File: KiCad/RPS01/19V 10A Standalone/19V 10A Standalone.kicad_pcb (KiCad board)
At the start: 2 copper layers, 33 parts, among them U2 LTC3780EUH-TRPBF

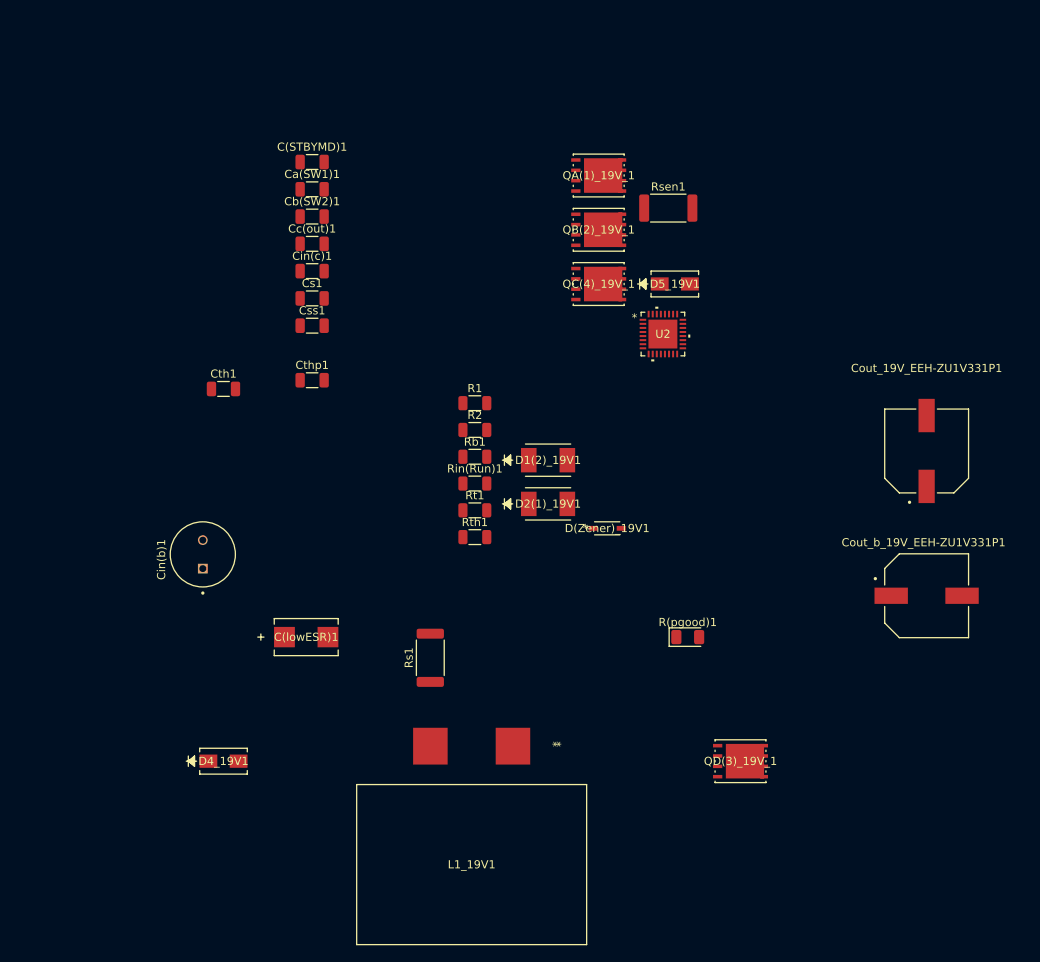
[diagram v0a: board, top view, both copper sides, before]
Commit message: 19V 10A Standalone PCB
Updated the standalone 19V 10A PCB. Just needs the connectors.
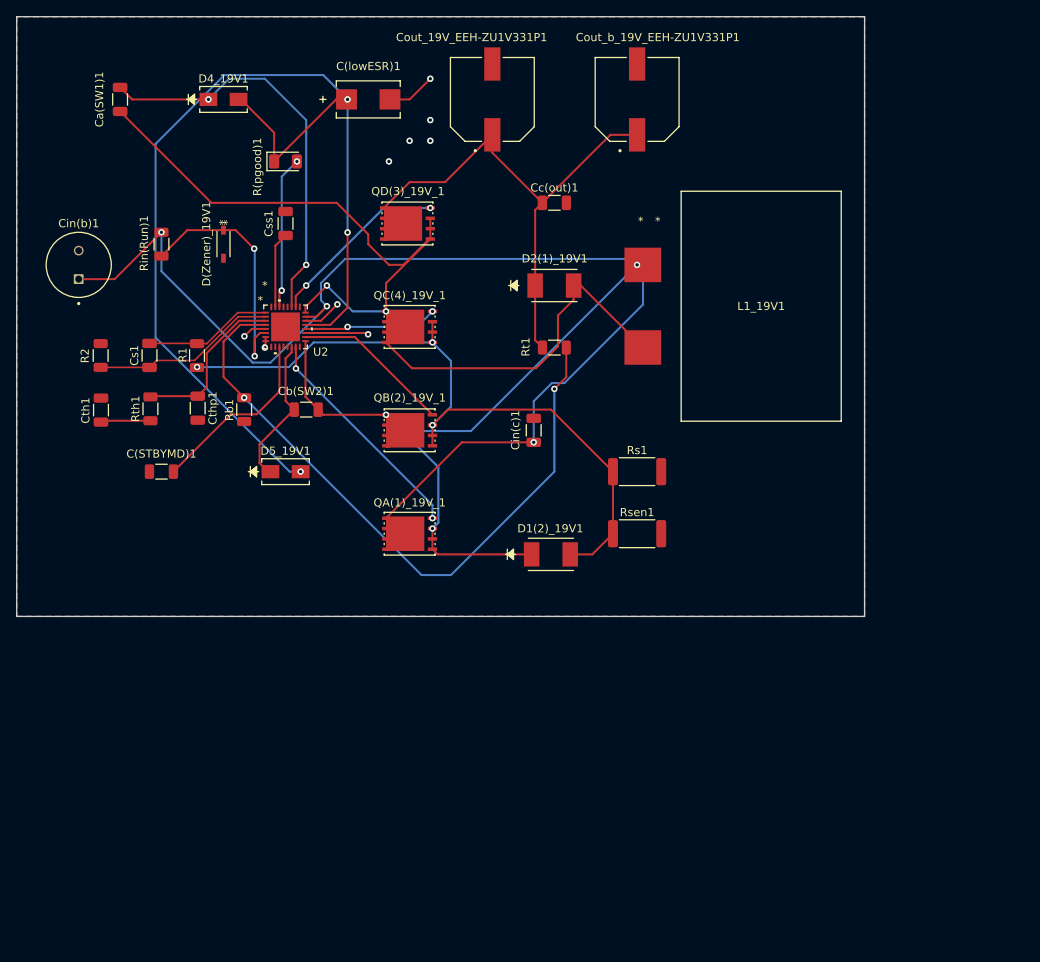
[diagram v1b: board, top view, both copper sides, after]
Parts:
- moved D4_19V1 81.3 mm to (114.3, 45.7)
- moved QD(3)_19V_1 77.7 mm to (136.9, 61.0), turned to 180 degrees
- moved L1_19V1 77.3 mm to (180.3, 71.1), turned to 0 degrees
- moved R(pgood)1 76.5 mm to (121.9, 53.3)
- moved Cout_b_19V_EEH-ZU1V331P1 70.6 mm to (165.1, 45.7), turned to 90 degrees
- moved Cout_19V_EEH-ZU1V331P1 68.6 mm to (147.3, 45.7)
- moved C(lowESR)1 66.5 mm to (132.1, 45.7)
- moved D(Zener)_19V1 58.6 mm to (114.3, 63.5), turned to -90 degrees
- moved D5_19V1 53.1 mm to (121.9, 91.4)
- moved QA(1)_19V_1 49.7 mm to (137.2, 99.1), turned to 180 degrees
- moved Rin(Run)1 48.4 mm to (106.7, 63.5), turned to -90 degrees
- moved R2 46.9 mm to (99.2, 77.2), turned to 90 degrees
- moved U2 46.4 mm to (121.9, 73.7)
- moved Rth1 42.8 mm to (105.3, 83.7), turned to 90 degrees
- moved C(STBYMD)1 42.3 mm to (106.7, 91.4), turned to 180 degrees
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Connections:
- Cb(SW2)1 pad 1: /BOOST2 -> /SW2
- D1(2)_19V1 pad 1: /BOOST2 -> /SW2
- L1_19V1 pad 1: /BOOST2 -> /SW2
- QA(1)_19V_1 pad 1: /BOOST2 -> /SW2
- QA(1)_19V_1 pad 2: /BOOST2 -> /SW2
- QA(1)_19V_1 pad 3: /BOOST2 -> /SW2
- QB(2)_19V_1 pad 5: /BOOST2 -> /SW2
- QB(2)_19V_1 pad 6: /BOOST2 -> /SW2
- QB(2)_19V_1 pad 7: /BOOST2 -> /SW2
- QB(2)_19V_1 pad 8: /BOOST2 -> /SW2
- U2 pad 17: /BOOST2 -> /SW2
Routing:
- net /Vin: track 0.00 -> 143.0 mm, vias 0 -> 3
- net /INTVCC: track 0.00 -> 130.0 mm, vias 0 -> 3
- net /SW1: track 0.00 -> 118.0 mm, vias 0 -> 2
- net /SW2: track 0.00 -> 89.7 mm, vias 0 -> 3
- net /Rsense: track 0.00 -> 87.3 mm, vias 0 -> 3
- net /VOSENSE: track 0.00 -> 82.2 mm, vias 0 -> 2
- net /Vout: track 0.00 -> 61.6 mm
- net /BOOST1: track 0.00 -> 50.3 mm, vias 0 -> 2
- net /Run: track 0.00 -> 30.7 mm, vias 0 -> 2
- net /TG2: track 0.00 -> 28.0 mm, vias 0 -> 2
- net /SENSE-: track 0.00 -> 22.8 mm
- net GND: track 0.00 -> 22.8 mm, vias 0 -> 9
- net /STBYMD: track 0.00 -> 22.6 mm
- net /TG1: track 0.00 -> 22.3 mm, vias 0 -> 2
- net /ITH: track 0.00 -> 20.5 mm
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- added copper zone on B.Cu, net GND
- added copper zone on F.Cu, net GND
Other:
- board outline added: 104.1 x 73.7 mm

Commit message: 19V 10A Standalone PCB
Final design of the Boost converter should be finished, double check if possible please!
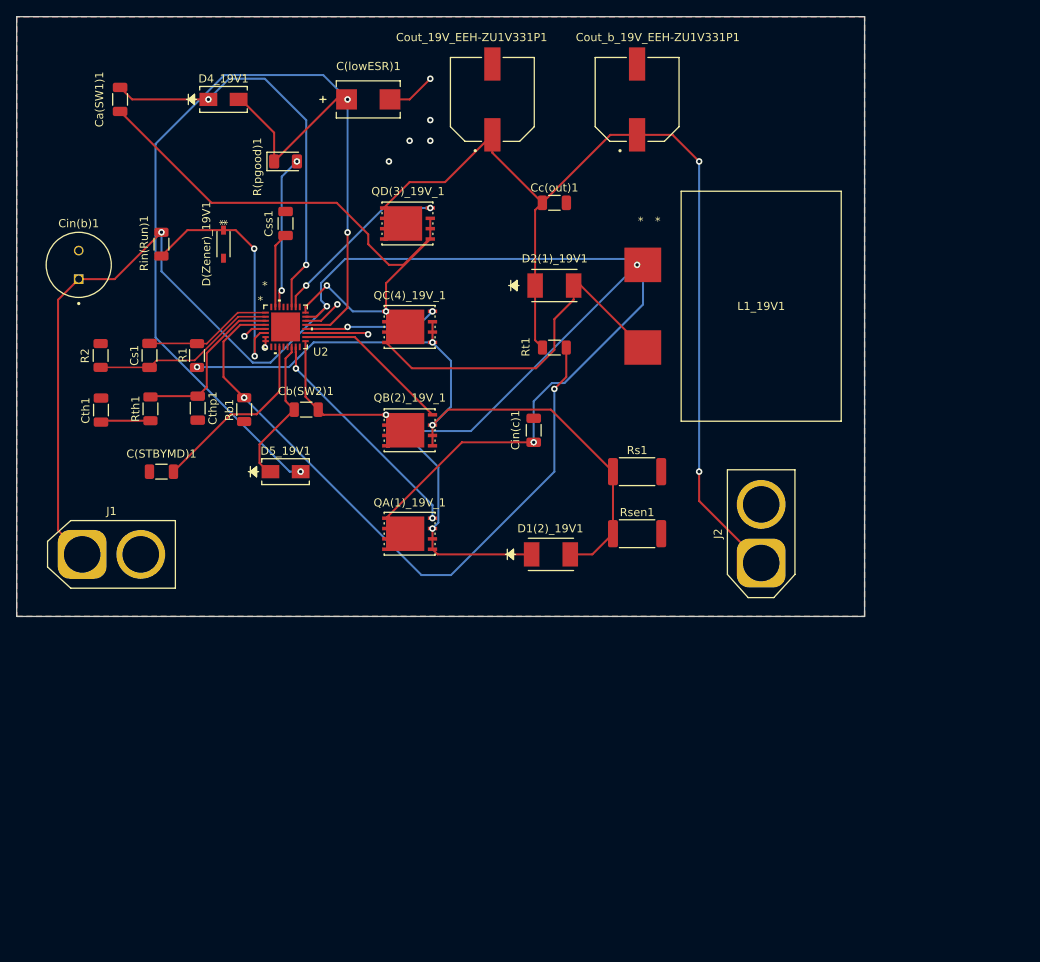
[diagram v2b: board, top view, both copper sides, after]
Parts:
- added J1: Conn_01x02_Socket, Mechatronic Footprints:AMASS_XT60-M_1x02_P7.20mm_Vertical, F.Cu at (96.9, 101.6)
- added J2: Conn_01x02_Socket, Mechatronic Footprints:AMASS_XT60-F_1x02_P7.20mm_Vertical, F.Cu at (180.3, 102.7)
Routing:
- net /Vout: track 61.6 -> 123.0 mm, vias 0 -> 2
- net /Vin: track 143.0 -> 179.1 mm

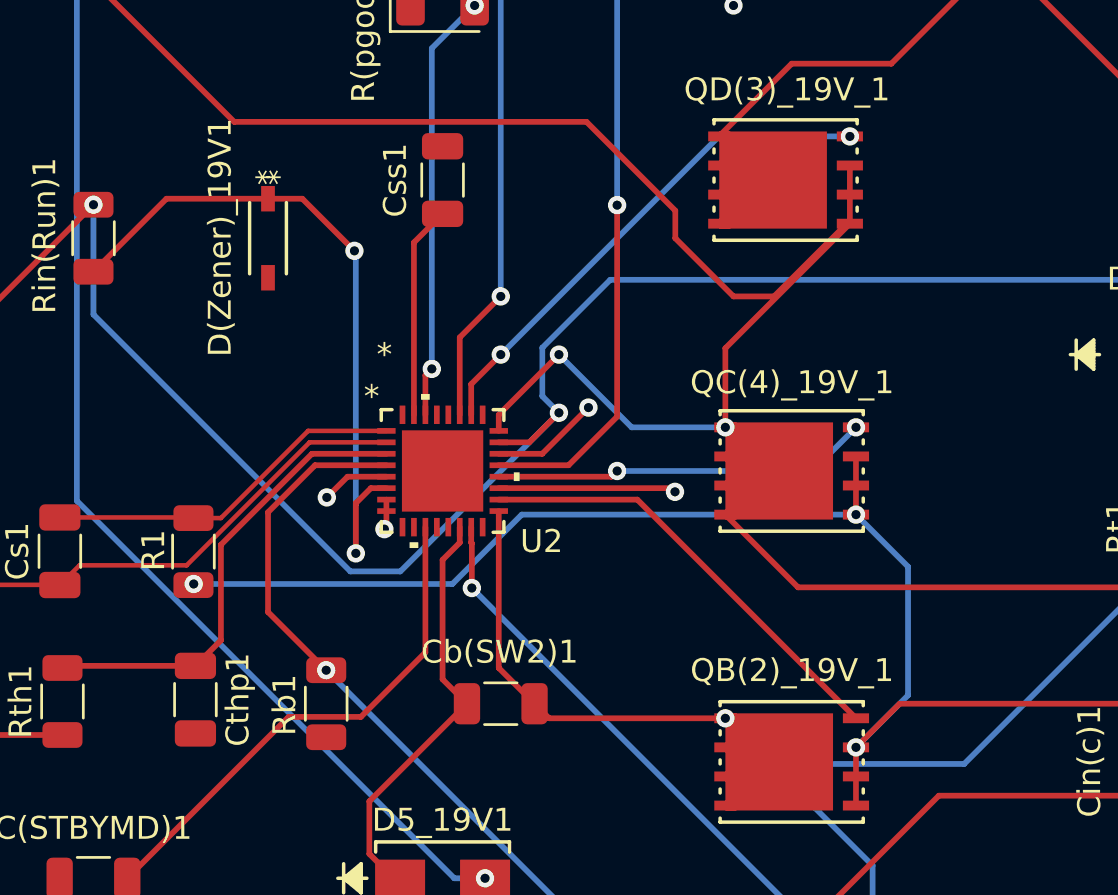
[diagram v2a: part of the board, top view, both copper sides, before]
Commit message: Update 19V 10A Standalone.kicad_pcb
Fixed Ground planes
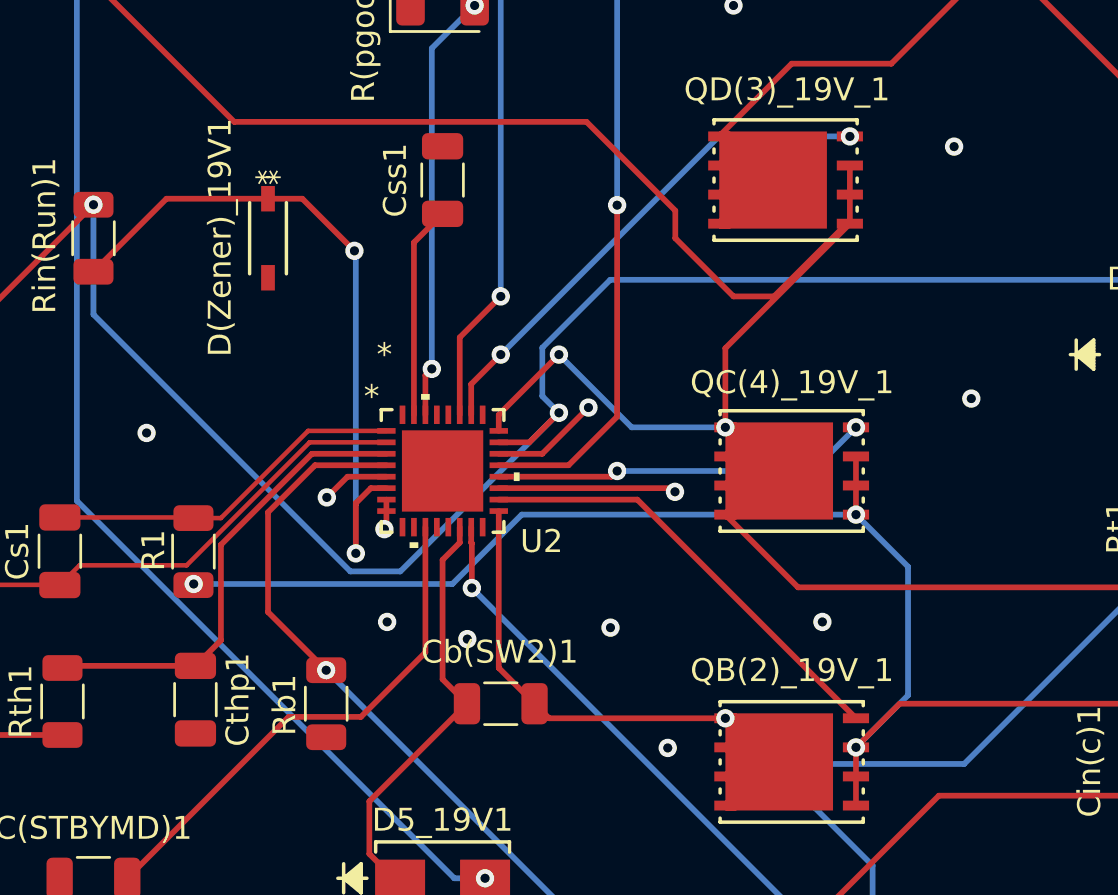
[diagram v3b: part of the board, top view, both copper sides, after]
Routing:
- net GND: vias 9 -> 17
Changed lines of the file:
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@@
   (segment (start 117.771242 73.91) (end 116.867155 74.814087) (width 0.25) (layer "F.Cu") (net 2))
   (segment (start 124.3724 74.410001) (end 131.906731 74.410001) (width 0.25) (layer "F.Cu") (net 2))
+  (via (at 119.5 80.25) (size 0.8) (drill 0.4) (layers "F.Cu" "B.Cu") (free) (net 2))
   (via (at 116.867155 74.814087) (size 0.8) (drill 0.4) (layers "F.Cu" "B.Cu") (free) (net 2))
   (via (at 137.16 50.8) (size 0.8) (drill 0.4) (layers "F.Cu" "B.Cu") (free) (net 2))
   (via (at 119.38 76.2) (size 0.8) (drill 0.4) (layers "F.Cu" "B.Cu") (free) (net 2))
+  (via (at 145 70.5) (size 0.8) (drill 0.4) (layers "F.Cu" "B.Cu") (free) (net 2))
+  (via (at 138.5 80.25) (size 0.8) (drill 0.4) (layers "F.Cu" "B.Cu") (free) (net 2))
   (via (at 128.28798 70.892579) (size 0.8) (drill 0.4) (layers "F.Cu" "B.Cu") (free) (net 2))
   (via (at 139.7 43.18) (size 0.8) (drill 0.4) (layers "F.Cu" "B.Cu") (free) (net 2))
   (via (at 139.7 50.8) (size 0.8) (drill 0.4) (layers "F.Cu" "B.Cu") (free) (net 2))
   (via (at 132.066422 74.569692) (size 0.8) (drill 0.4) (layers "F.Cu" "B.Cu") (free) (net 2))
+  (via (at 123 81) (size 0.8) (drill 0.4) (layers "F.Cu" "B.Cu") (free) (net 2))
   (via (at 134.62 53.34) (size 0.8) (drill 0.4) (layers "F.Cu" "B.Cu") (free) (net 2))
+  (via (at 131.75 85.75) (size 0.8) (drill 0.4) (layers "F.Cu" "B.Cu") (free) (net 2))
+  (via (at 109 72) (size 0.8) (drill 0.4) (layers "F.Cu" "B.Cu") (free) (net 2))
+  (via (at 144.25 59.5) (size 0.8) (drill 0.4) (layers "F.Cu" "B.Cu") (free) (net 2))
+  (via (at 129.25 80.5) (size 0.8) (drill 0.4) (layers "F.Cu" "B.Cu") (free) (net 2))
   (via (at 139.7 48.26) (size 0.8) (drill 0.4) (layers "F.Cu" "B.Cu") (free) (net 2))
   (segment (start 118.355 84.395) (end 121.169999 81.580001) (width 0.25) (layer "F.Cu") (net 3))

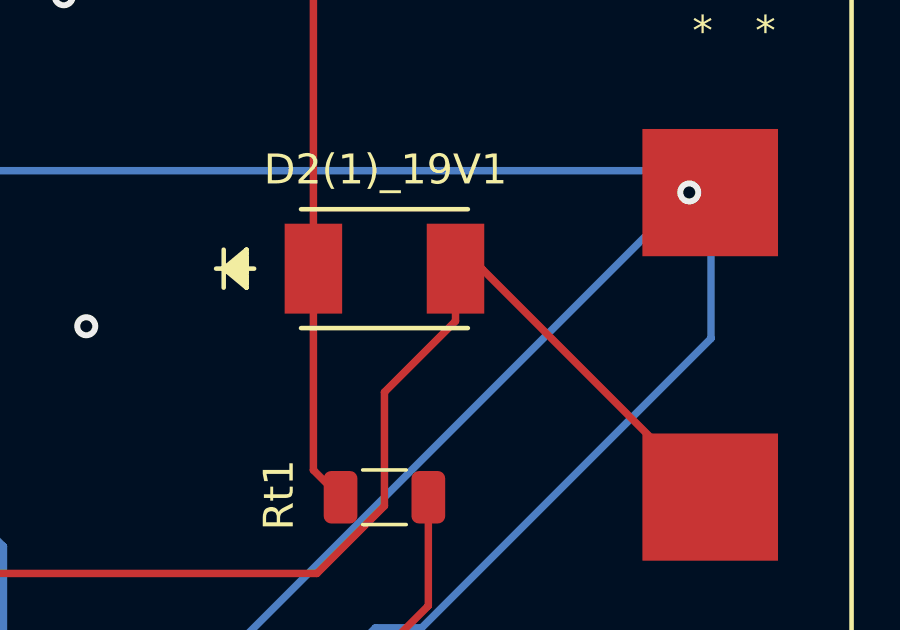
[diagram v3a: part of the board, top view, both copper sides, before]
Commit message: fixzed super bad issue on ground plane
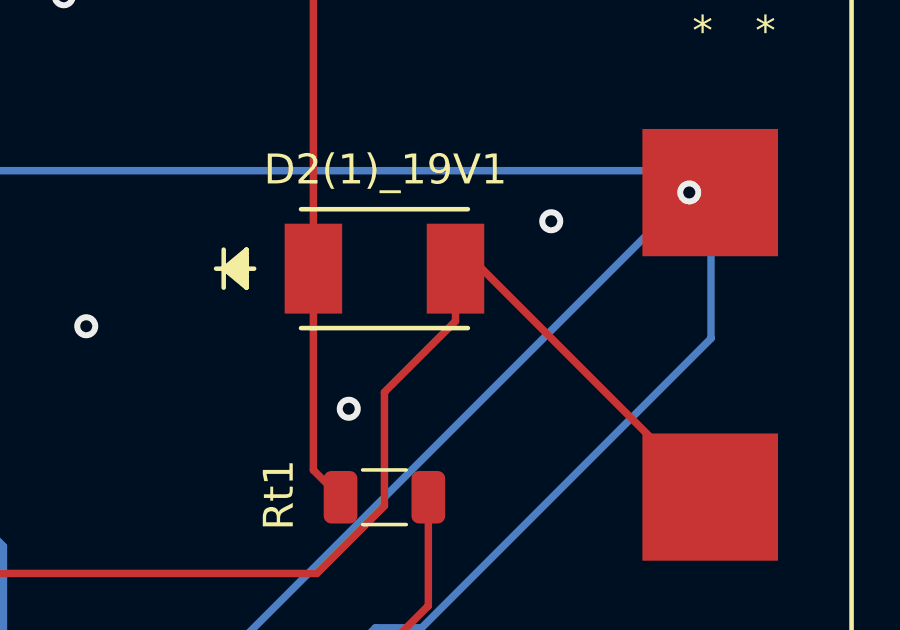
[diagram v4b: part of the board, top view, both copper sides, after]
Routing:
- net GND: vias 17 -> 19
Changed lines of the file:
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@@
   (via (at 128.28798 70.892579) (size 0.8) (drill 0.4) (layers "F.Cu" "B.Cu") (free) (net 2))
   (via (at 139.7 43.18) (size 0.8) (drill 0.4) (layers "F.Cu" "B.Cu") (free) (net 2))
+  (via (at 153.75 73.25) (size 0.8) (drill 0.4) (layers "F.Cu" "B.Cu") (free) (net 2))
   (via (at 139.7 50.8) (size 0.8) (drill 0.4) (layers "F.Cu" "B.Cu") (free) (net 2))
+  (via (at 160.5 67) (size 0.8) (drill 0.4) (layers "F.Cu" "B.Cu") (free) (net 2))
   (via (at 132.066422 74.569692) (size 0.8) (drill 0.4) (layers "F.Cu" "B.Cu") (free) (net 2))
   (via (at 123 81) (size 0.8) (drill 0.4) (layers "F.Cu" "B.Cu") (free) (net 2))
